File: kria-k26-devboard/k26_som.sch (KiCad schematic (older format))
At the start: 15 parts, among them M1 XILINX-KRIA-K26

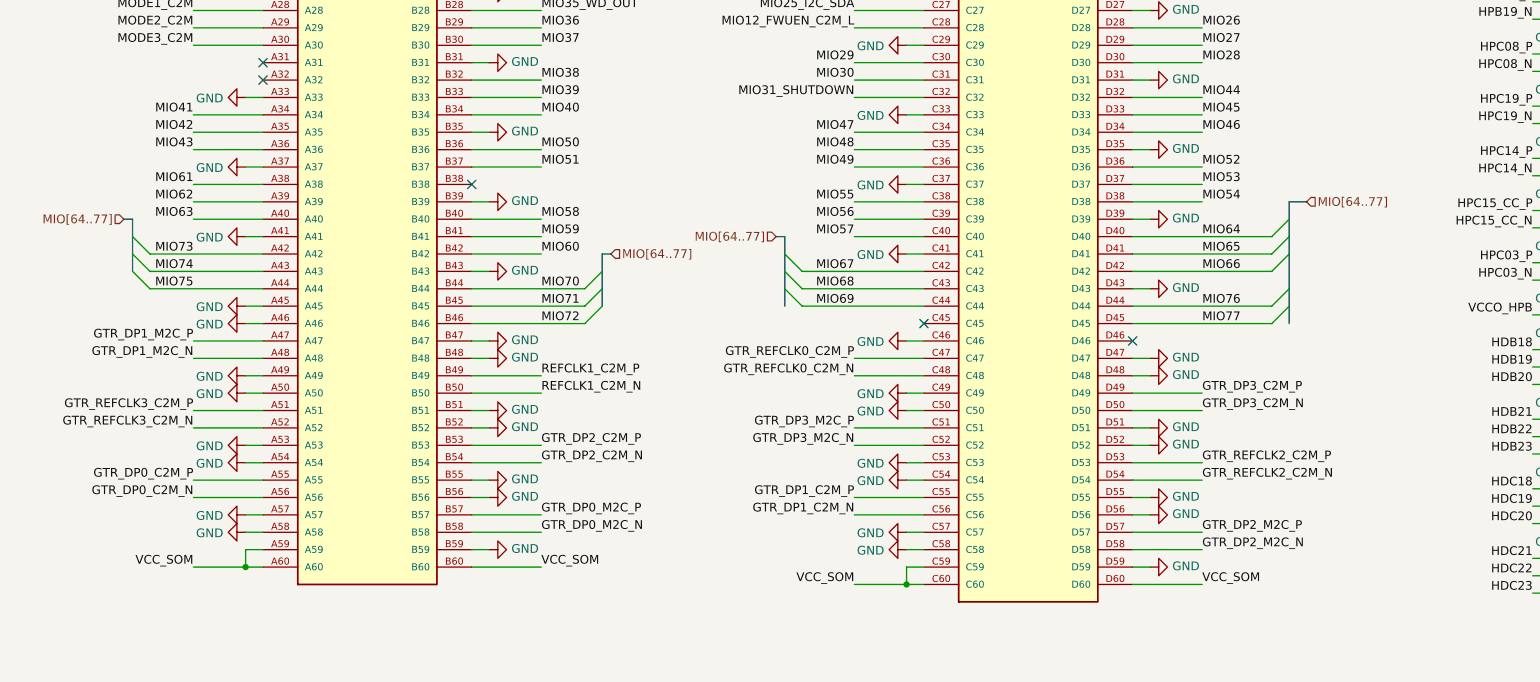
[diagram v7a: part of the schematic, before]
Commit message: Added and connected USB PHY and HUB, created schematic sheet for PCIE M2 key E
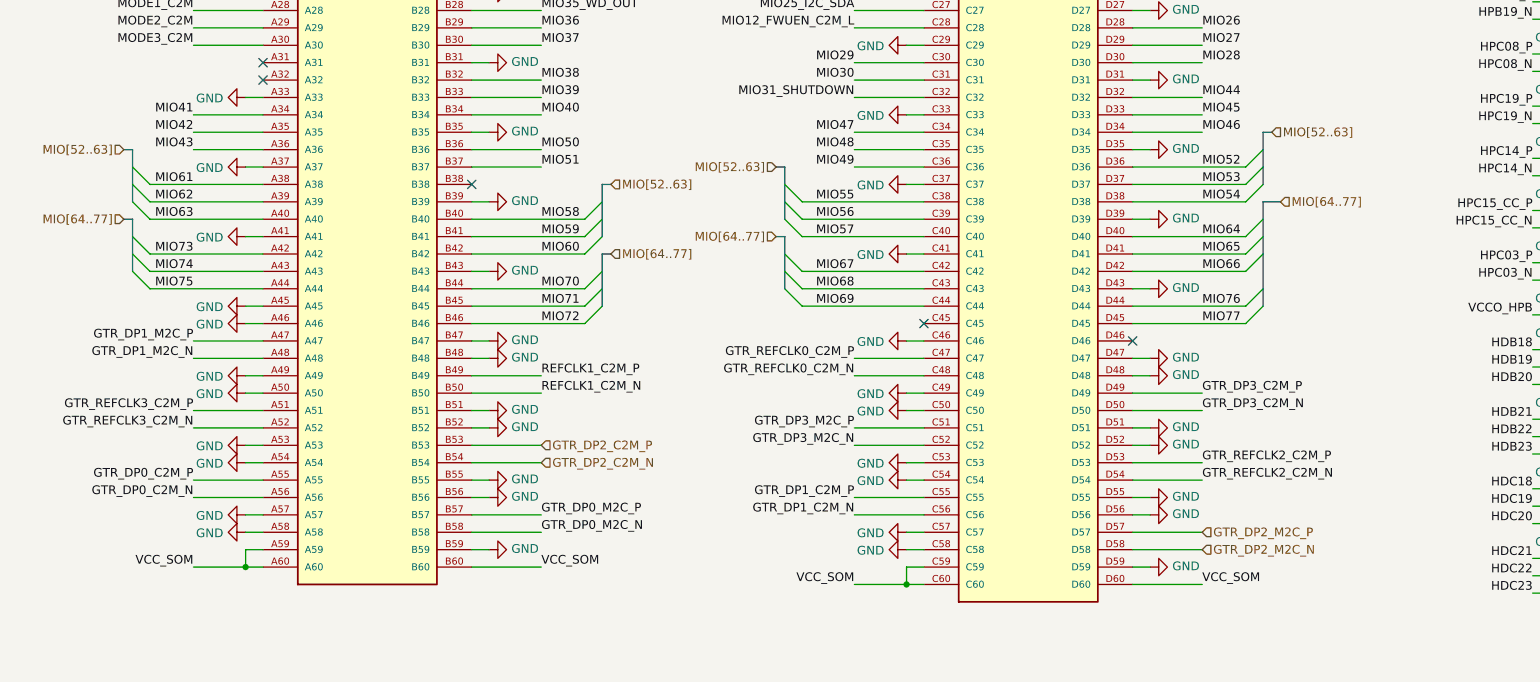
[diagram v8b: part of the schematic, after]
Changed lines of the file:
@@
 $Descr A3 16535 11693
 encoding utf-8
-Sheet 2 13
+Sheet 2 14
 Title "K26 SOM connnector"
 Date "2022-03-10"
@@
 Text Label 1400 6300 2    50   ~ 0
 MIO62
-Wire Wire Line
-	1800 6300 1400 6300
 Text Label 1400 6200 2    50   ~ 0
 MIO61
-Wire Wire Line
-	1800 6200 1400 6200
 Text Label 1400 6400 2    50   ~ 0
 MIO63
 Wire Wire Line
-	1800 6400 1400 6400
-Wire Wire Line
 	1800 6500 1700 6500
 Text Label 1400 6700 2    50   ~ 0
@@
 	0    -1   -1   0
 $EndComp
-Wire Wire Line
-	3000 6400 3400 6400
 Text Label 3400 6400 0    50   ~ 0
 MIO58
-Wire Wire Line
-	3000 6600 3400 6600
 Text Label 3400 6600 0    50   ~ 0
 MIO60
-Wire Wire Line
-	3000 6500 3400 6500
 Text Label 3400 6500 0    50   ~ 0
 MIO59
@@
 Wire Wire Line
 	3000 7800 3400 7800
-Text Label 3400 7800 0    50   ~ 0
-GTR_DP2_C2M_N
 Wire Wire Line
 	3000 7700 3400 7700
-Text Label 3400 7700 0    50   ~ 0
-GTR_DP2_C2M_P
 Wire Wire Line
 	3000 8200 3400 8200
@@
 	0    1    1    0
 $EndComp
-Wire Wire Line
-	5600 6500 5200 6500
 Text Label 5200 6500 2    50   ~ 0
 MIO57
-Wire Wire Line
-	5600 6300 5200 6300
 Text Label 5200 6300 2    50   ~ 0
 MIO55
-Wire Wire Line
-	5600 6400 5200 6400
 Text Label 5200 6400 2    50   ~ 0
 MIO56
@@
 MIO53
 Wire Wire Line
-	6800 6100 7200 6100
-Wire Wire Line
-	7200 6200 6800 6200
-Wire Wire Line
 	6800 6000 6900 6000
 $Comp
@@
 Wire Wire Line
 	6800 8400 6900 8400
-Text Label 7200 8200 0    50   ~ 0
-GTR_DP2_M2C_P
 Text Label 7200 8500 0    50   ~ 0
 VCC_SOM
-Text Label 7200 8300 0    50   ~ 0
-GTR_DP2_M2C_N
 Wire Wire Line
 	6800 8500 7200 8500
 Text Label 7200 6300 0    50   ~ 0
 MIO54
-Wire Wire Line
-	7200 6300 6800 6300
 $Comp
 L power:GND #PWR0174
@@
 Text Notes 1200 10100 0    50   ~ 0
 SOM 5V0 decoupling
-Text HLabel 7800 6300 2    50   Input ~ 0
+Text HLabel 7650 6300 2    50   Input ~ 0
 MIO[64..77]
 Wire Bus Line
-	7800 6300 7700 6300
+	7650 6300 7550 6300
 Entry Wire Line
-	7600 6500 7700 6400
+	7450 6500 7550 6400
 Wire Wire Line
-	6800 6500 7600 6500
+	6800 6500 7450 6500
 Wire Wire Line
-	6800 6600 7600 6600
+	6800 6600 7450 6600
 Wire Wire Line
-	6800 6700 7600 6700
+	6800 6700 7450 6700
 Wire Wire Line
-	6800 6900 7600 6900
+	6800 6900 7450 6900
 Wire Wire Line
-	6800 7000 7600 7000
+	6800 7000 7450 7000
 Entry Wire Line
-	7600 6900 7700 6800
+	7450 6900 7550 6800
 Entry Wire Line
-	7600 7000 7700 6900
+	7450 7000 7550 6900
 Entry Wire Line
-	7600 6700 7700 6600
+	7450 6700 7550 6600
 Entry Wire Line
-	7600 6600 7700 6500
+	7450 6600 7550 6500
 Text HLabel 3800 6600 2    50   Input ~ 0
 MIO[64..77]
@@
 Text HLabel 4750 6500 0    50   Input ~ 0
 MIO[64..77]
+Text HLabel 1400 4400 0    50   Input ~ 0
+VCCO_EN_PL_M2C
+Text HLabel 1400 4300 0    50   Input ~ 0
+VCCO_EN_PS_M2C
+Text HLabel 3800 6200 2    50   Input ~ 0
+MIO[52..63]
+Entry Wire Line
+	3650 6400 3750 6300
+Entry Wire Line
+	3650 6500 3750 6400
+Entry Wire Line
+	3650 6600 3750 6500
+Wire Bus Line
+	3750 6200 3800 6200
+Wire Wire Line
+	3000 6600 3650 6600
+Wire Wire Line
+	3000 6500 3650 6500
+Wire Wire Line
+	3000 6400 3650 6400
+Text HLabel 1000 6000 0    50   Input ~ 0
+MIO[52..63]
+Entry Wire Line
+	1150 6200 1050 6100
+Entry Wire Line
+	1150 6300 1050 6200
+Entry Wire Line
+	1150 6400 1050 6300
+Wire Bus Line
+	1050 6000 1000 6000
+Wire Wire Line
+	1150 6400 1800 6400
+Wire Wire Line
+	1150 6300 1800 6300
+Wire Wire Line
+	1150 6200 1800 6200
+Text HLabel 4750 6100 0    50   Input ~ 0
+MIO[52..63]
+Entry Wire Line
+	4900 6300 4800 6200
+Entry Wire Line
+	4900 6400 4800 6300
+Entry Wire Line
+	4900 6500 4800 6400
+Wire Bus Line
+	4800 6100 4750 6100
+Wire Wire Line
+	4900 6300 5600 6300
+Wire Wire Line
+	4900 6400 5600 6400
+Wire Wire Line
+	4900 6500 5600 6500
+Text HLabel 7600 5900 2    50   Input ~ 0
+MIO[52..63]
+Entry Wire Line
+	7450 6100 7550 6000
+Entry Wire Line
+	7450 6200 7550 6100
+Entry Wire Line
+	7450 6300 7550 6200
+Wire Bus Line
+	7550 5900 7600 5900
+Wire Wire Line
+	6800 6300 7450 6300
+Wire Wire Line
+	6800 6200 7450 6200
+Wire Wire Line
+	6800 6100 7450 6100
+Wire Bus Line
+	4800 6500 4800 6800
 Wire Bus Line
 	3750 6600 3750 6900
@@
 	1050 6400 1050 6700
 Wire Bus Line
-	4800 6500 4800 6900
+	3750 6200 3750 6500
 Wire Bus Line
-	7700 6300 7700 7000
-Text HLabel 1400 4400 0    50   Input ~ 0
-VCCO_EN_PL_M2C
-Text HLabel 1400 4300 0    50   Input ~ 0
-VCCO_EN_PS_M2C
+	1050 6000 1050 6300
+Wire Bus Line
+	4800 6100 4800 6400
+Wire Bus Line
+	7550 5900 7550 6200
+Wire Bus Line
+	7550 6300 7550 6900
+Text HLabel 3400 7700 2    50   Input ~ 0
+GTR_DP2_C2M_P
+Text HLabel 3400 7800 2    50   Input ~ 0
+GTR_DP2_C2M_N
+Text HLabel 7200 8200 2    50   Input ~ 0
+GTR_DP2_M2C_P
+Text HLabel 7200 8300 2    50   Input ~ 0
+GTR_DP2_M2C_N
 $EndSCHEMATC
